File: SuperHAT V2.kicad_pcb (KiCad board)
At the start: 4 copper layers, 65 x 56.5 mm, 66 parts, among them J1 GPIO, J10 Qwiic_RA, J11 BM02B-GHS-TBT_LF__SN_, J13 SM02B-PASS-TBTLFSN, J2 Conn_01x03, J4 Conn_01x03, J5 Qwiic_RA, J6 Qwiic_Vertical, J7 Qwiic_Vertical, J8 SM04B-GHS-TB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

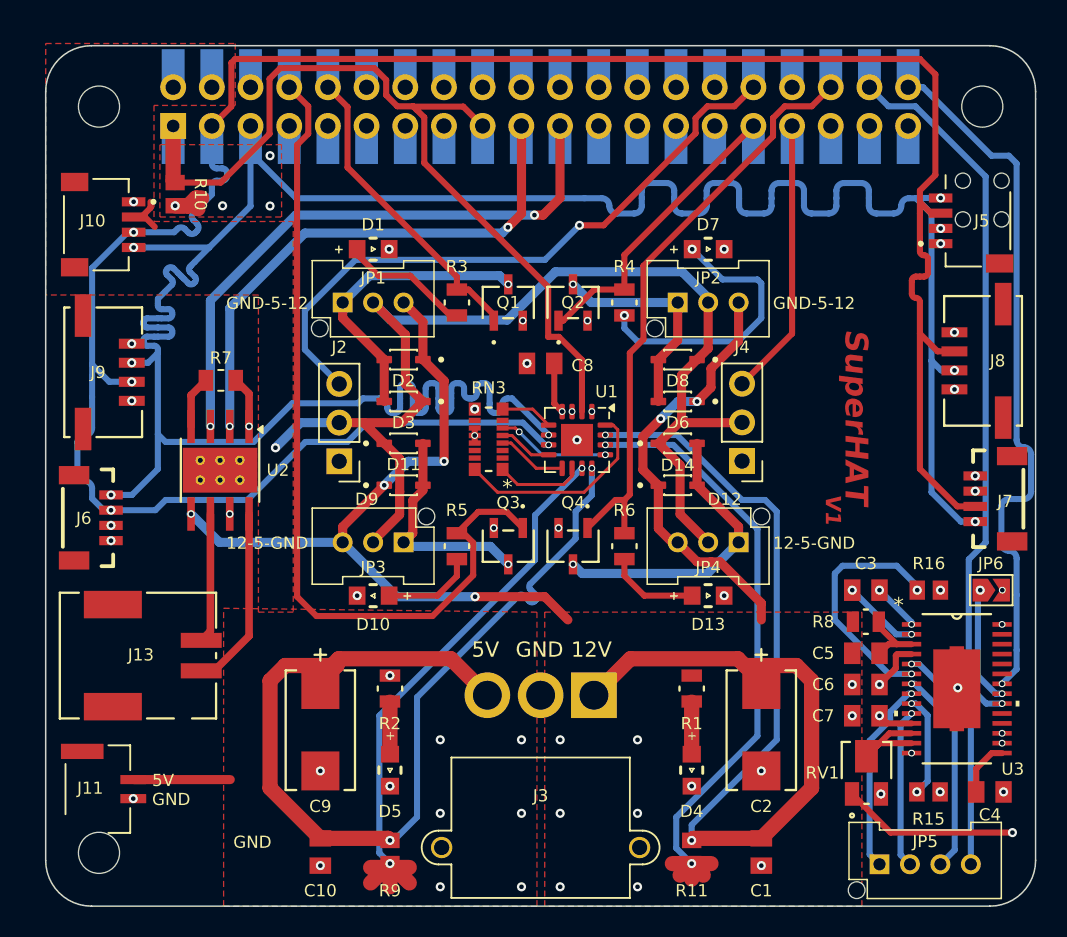
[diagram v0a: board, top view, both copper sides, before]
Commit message: Fixed MOSFET circuits, pin values, and diode layout.
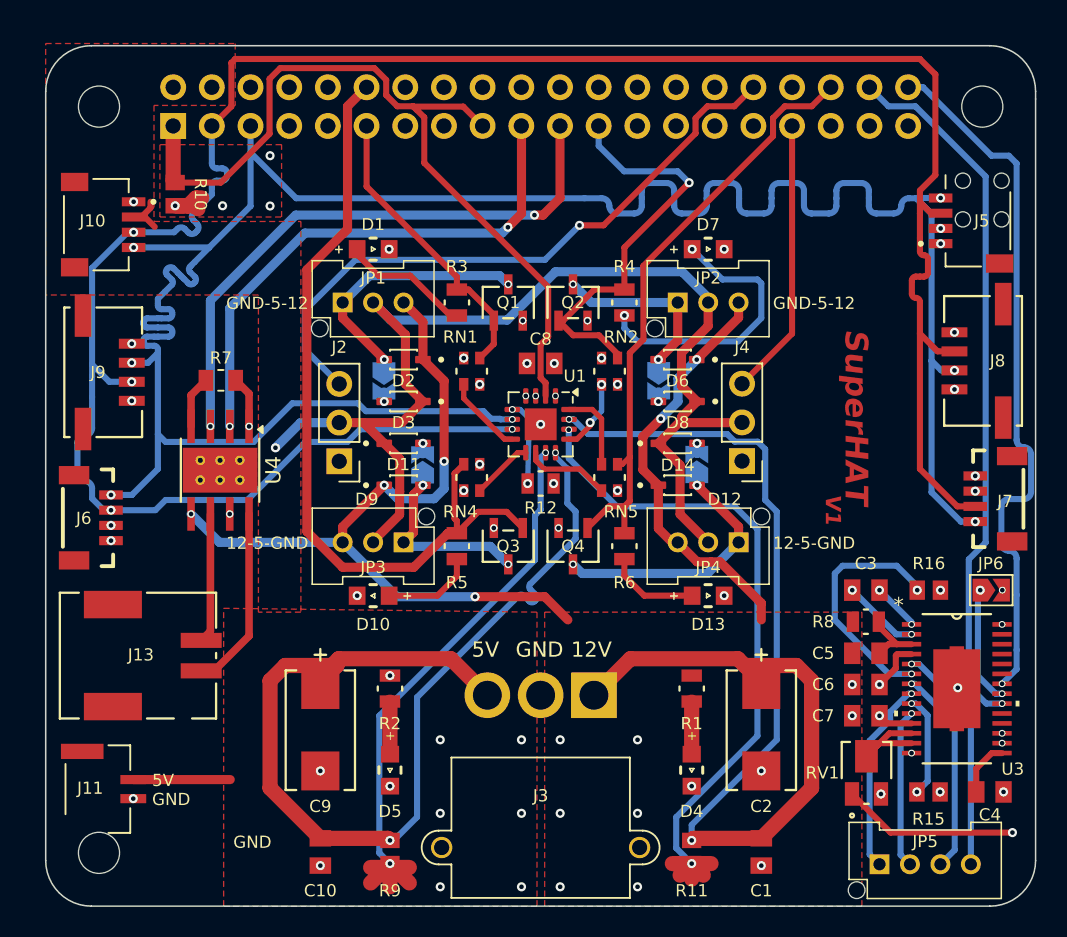
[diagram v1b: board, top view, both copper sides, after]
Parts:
- removed RN3: 10k, 10k Resistor Array:RES_EXB2HV
- removed U2: DRV8871DDA, Package_SO:Texas_HTSOP-8-1EP_3.9x4.9mm_P1.27mm_EP2.95x4.9mm_Mask2.4x3.1mm_ThermalVias
- added JP10: SolderJumper_2_Open, Jumper:SolderJumper-2_P1.3mm_Open_TrianglePad1.0x1.5mm, B.Cu at (142.8, 71.0)
- added JP7: SolderJumper_2_Open, Jumper:SolderJumper-2_P1.3mm_Open_TrianglePad1.0x1.5mm, B.Cu at (122.2, 65.5)
- added JP8: SolderJumper_2_Open, Jumper:SolderJumper-2_P1.3mm_Open_TrianglePad1.0x1.5mm, B.Cu at (140.2, 65.5)
- added JP9: SolderJumper_2_Open, Jumper:SolderJumper-2_P1.3mm_Open_TrianglePad1.0x1.5mm, B.Cu at (124.8, 71.0)
- added R12: 10k, 0805 Resistor Moisture Resistant:RES_CHP0805_BRN, F.Cu at (132.5, 72.2)
- added RN1: 10k, 2 RES 10k Array:SMT_1002P1AT_VIS, F.Cu at (128.0, 64.9)
- added RN2: 10k, 2 RES 10k Array:SMT_1002P1AT_VIS, F.Cu at (137.0, 64.9)
- added RN4: 10k, 2 RES 10k Array:SMT_1002P1AT_VIS, F.Cu at (128.0, 71.8)
- added RN5: 10k, 2 RES 10k Array:SMT_1002P1AT_VIS, F.Cu at (137.0, 71.8)
- added U4: DRV8871DDA, Package_SO:Texas_HTSOP-8-1EP_3.9x4.9mm_P1.27mm_EP2.95x4.9mm_Mask2.4x3.1mm_ThermalVias, F.Cu at (111.5, 71.4)
- moved D6 2.75 mm to (141.5, 64.1)
- moved D8 2.75 mm to (141.5, 66.9)
- moved U1 2.60 mm to (132.5, 68.4)
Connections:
- D11 pad A: Net-(Q3-D) -> Net-(JP9-B)
- D12 pad A: Net-(Q4-D) -> Net-(JP10-A)
- D14 pad A: Net-(Q4-D) -> Net-(JP10-B)
- D2 pad A: Net-(Q1-D) -> Net-(JP7-A)
- D3 pad A: Net-(Q1-D) -> Net-(JP7-B)
- D6 pad A: Net-(Q2-D) -> Net-(JP8-A)
- D8 pad A: Net-(Q2-D) -> Net-(JP8-B)
- D9 pad A: Net-(Q3-D) -> Net-(JP9-A)
- J1 pad 10: GPIO15/RXD0 -> /GPIO15/RXD0
- J1 pad 11: /GPIO17 -> GPIO17
- J1 pad 12: /GPIO18/PCM.CLK -> GPIO18/PCM.CLK
- J1 pad 23: /GPIO11/SPI0.SCLK -> GPIO11/SPI0.SCLK
- J1 pad 31: GPIO6 -> /GPIO6
- J1 pad 8: GPIO14/TXD0 -> /GPIO14/TXD0
- JP1 pad 1: Net-(Q1-D) -> Net-(JP7-A)
- JP2 pad 1: Net-(Q2-D) -> Net-(JP8-A)
- JP3 pad 1: Net-(Q3-D) -> Net-(JP9-A)
- JP4 pad 1: Net-(Q4-D) -> Net-(JP10-A)
- Q1 pad 1: GPIO15/RXD0 -> GPIO17
- Q1 pad 3: Net-(Q1-D) -> Net-(JP7-A)
- Q2 pad 1: GPIO6 -> GPIO11/SPI0.SCLK
- Q2 pad 3: Net-(Q2-D) -> Net-(JP8-A)
- Q3 pad 1: GPIO14/TXD0 -> GPIO18/PCM.CLK
- Q3 pad 3: Net-(Q3-D) -> Net-(JP9-A)
- Q4 pad 3: Net-(Q4-D) -> Net-(JP10-A)
- R3 pad 1: GPIO15/RXD0 -> GPIO17
- R4 pad 1: GPIO6 -> GPIO11/SPI0.SCLK
- R5 pad 1: GPIO14/TXD0 -> GPIO18/PCM.CLK
- U1 pad 10: Net-(RN3-R1.1) -> /PV
- U1 pad 13: Net-(RN3-R6.1) -> /TC
- U1 pad 16: Net-(RN3-R1.2) -> /VPU
- U1 pad 8: Net-(RN3-R5.1) -> /WARNING
- U1 pad 9: Net-(RN3-R4.1) -> /CRITICAL
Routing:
- net GPIO14/TXD0: track 56.3 -> 0.00 mm
- net GPIO18/PCM.CLK: track 0.00 -> 53.2 mm
- net GPIO11/SPI0.SCLK: track 0.00 -> 27.2 mm, vias 0 -> 1
- net GPIO15/RXD0: track 20.3 -> 0.00 mm
- net Net-(Q4-D): track 19.6 -> 0.00 mm, vias 1 -> 0
- net GPIO17: track 0.00 -> 19.5 mm
- net Net-(Q1-D): track 19.5 -> 0.00 mm, vias 1 -> 0
- net GPIO6: track 19.4 -> 0.00 mm
- net Net-(JP10-A): track 0.00 -> 17.5 mm, vias 0 -> 2
- net Net-(JP7-A): track 0.00 -> 17.4 mm, vias 0 -> 2
- net Net-(Q3-D): track 14.5 -> 0.00 mm, vias 1 -> 0
- net Net-(Q2-D): track 14.4 -> 0.00 mm, vias 1 -> 0
- net /GPIO3/SCL1: track 169.6 -> 155.3 mm
- net Net-(RN3-R1.2): track 13.8 -> 0.00 mm
- net Net-(JP9-A): track 0.00 -> 12.4 mm, vias 0 -> 2
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
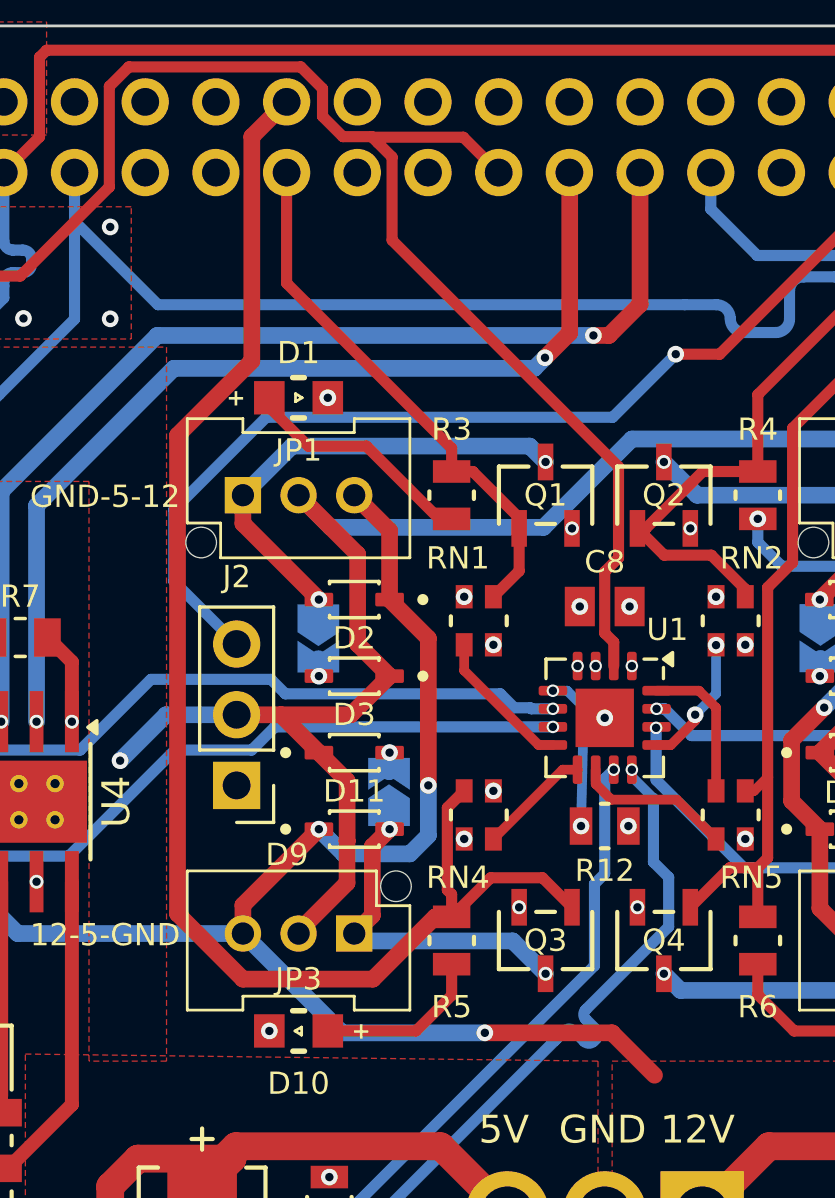
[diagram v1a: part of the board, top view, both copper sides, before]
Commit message: Added overvoltage protection to schematic.
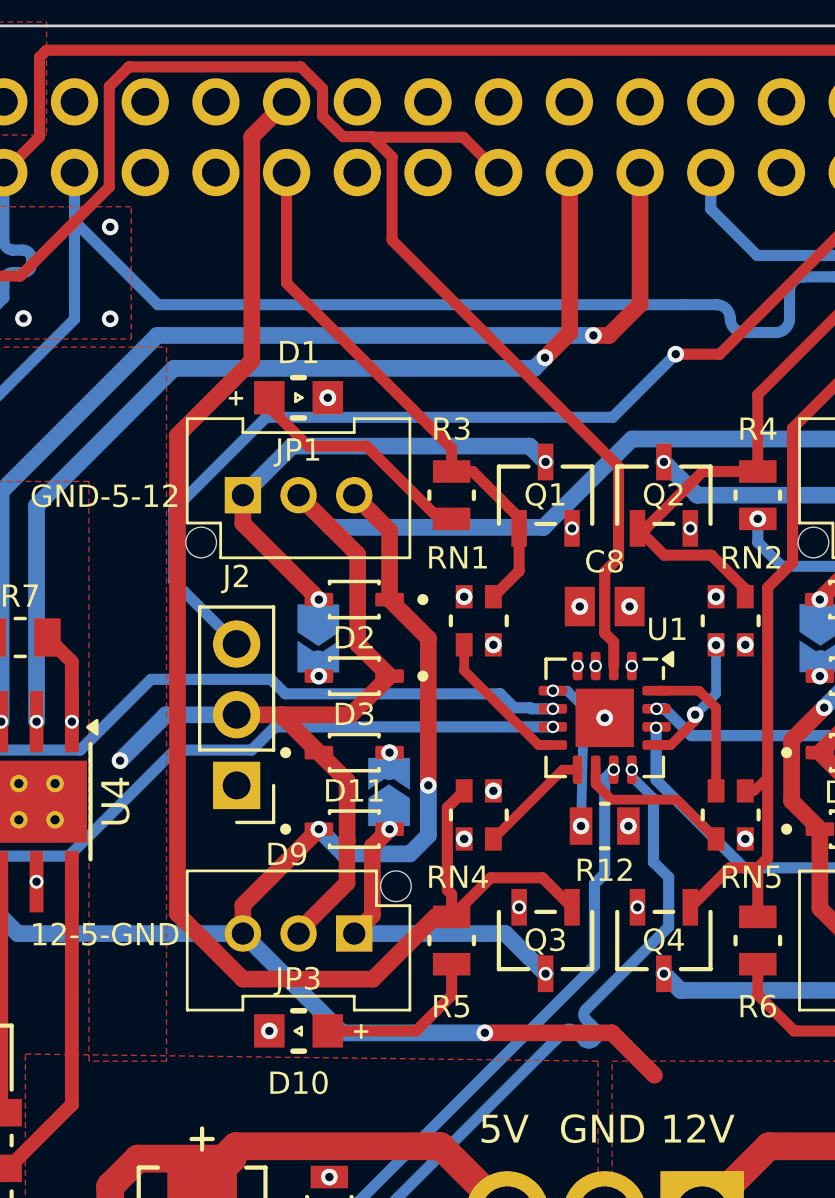
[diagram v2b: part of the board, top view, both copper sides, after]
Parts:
- R3, R4, R5, R6: value 33 -> 100; footprint CMP0805AFX:RES_CMP0805_BRN -> 0805 Resistor Moisture Resistant:RES_CHP0805_BRN

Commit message: Overvoltage protection laid out on footprint.
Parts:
- removed J13: SM02B-PASS-TBTLFSN, SM02B-PASS-TBT:CONN_SM02B-PASS_JST
- added C11: 10 nF, 0805 Ceramic Capacitor:CAPC2012X140N, F.Cu at (108.0, 91.5)
- added C12: 0.1 uF, 0805 Ceramic Capacitor:CAPC2012X140N, F.Cu at (108.5, 57.1)
- added J12: B02B-PASK-1, B02B-PASK-1:CONN_B02B-PASK-1_JST, F.Cu at (104.2, 83.0)
- added R13: 10k, 0805 Resistor Moisture Resistant:RES_CHP0805_BRN, F.Cu at (102.9, 98.2)
- added R14: 453, RESC2012X60N:RESC2012X60N, F.Cu at (107.2, 98.2)
- added R17: 470k, CMP0805AFX:RES_CMP0805_BRN, F.Cu at (108.0, 95.2)
- added R18: 7.5k, TNPW0805:RES_TNPW0805_VIS, F.Cu at (102.9, 88.3)
- added R19: 2.4k, TNPW0805:RES_TNPW0805_VIS, F.Cu at (107.3, 88.3)
- added U2: TPS259631DDAR, TPS259631:SOIC_20DDAR_TEX, F.Cu at (103.8, 93.3)
- J11: value BM02B-GHS-TBT_LF__SN_ -> Conn_01x02; footprint BM02B-GHS-TBT:BM02B-GHS-TBT -> Connector_PinHeader_2.54mm:PinHeader_1x02_P2.54mm_Horizontal
- moved J11 13.1 mm to (115.0, 95.6)
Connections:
- J1 pad 2: +5V -> +5VPI
- J1 pad 4: +5V -> +5VPI
- J10 pad 2: +5V -> +5VPI
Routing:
- net /GPIO27: track 0.00 -> 82.5 mm, vias 0 -> 1
- net +5V: track 125.7 -> 114.6 mm
- net Net-(U2-EN/UVLO): track 0.00 -> 5.02 mm
- net Net-(U2-DVDT): track 0.00 -> 4.49 mm
- net +3V3: track 15.1 -> 19.4 mm, vias 19 -> 21
- net Net-(U2-ILM): track 0.00 -> 2.98 mm
- net Net-(U4-OUT1): track 8.55 -> 10.9 mm
- net Net-(U2-OVCSEL): track 0.00 -> 2.25 mm
- net Net-(U4-OUT2): track 12.1 -> 14.0 mm
- net GND: track 3.39 -> 4.89 mm, vias 40 -> 46
- net +5VPI: track 0.00 -> 1.25 mm
- added copper zone on F.Cu, net +5VPI
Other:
- outline, holes or cut-outs redrawn
- board text added: "V2"

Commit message: Pre footprint migration to create BOM V2
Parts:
- R1: value 1k -> 3k; footprint 0805 Resistor Moisture Resistant:RES_CHP0805_BRN -> TNPW0805:RES_TNPW0805_VIS
- R2: value 330 -> 1k; footprint 0805 330 Ohm Resistor Moisture Resistant:RES_CMP0805_BRN -> TNPW0805:RES_TNPW0805_VIS
- moved R1 0.29 mm to (142.4, 86.0)
- moved R2 0.29 mm to (122.6, 86.0)
- moved D4 0.22 mm to (142.4, 91.3)
- moved D5 0.22 mm to (122.6, 91.3)
- moved D10 0.20 mm to (121.5, 79.8)
- moved D13 0.20 mm to (143.5, 79.8)
- moved D1 0.20 mm to (121.5, 56.7)
- moved D7 0.20 mm to (143.5, 56.7)
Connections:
- U3 pad 20: /GPIO20/PCM.DIN -> /GPIO26
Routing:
- net /GPIO20/PCM.DIN: track 46.6 -> 0.00 mm, vias 1 -> 0
- net /GPIO26: track 0.00 -> 44.3 mm, vias 0 -> 1
- net /GPIO3/SCL1: track 155.3 -> 167.1 mm
- net +5VPI: track 1.25 -> 8.03 mm
- net +12V: track 130.4 -> 131.6 mm, vias 16 -> 17
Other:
- board text removed: "V1"

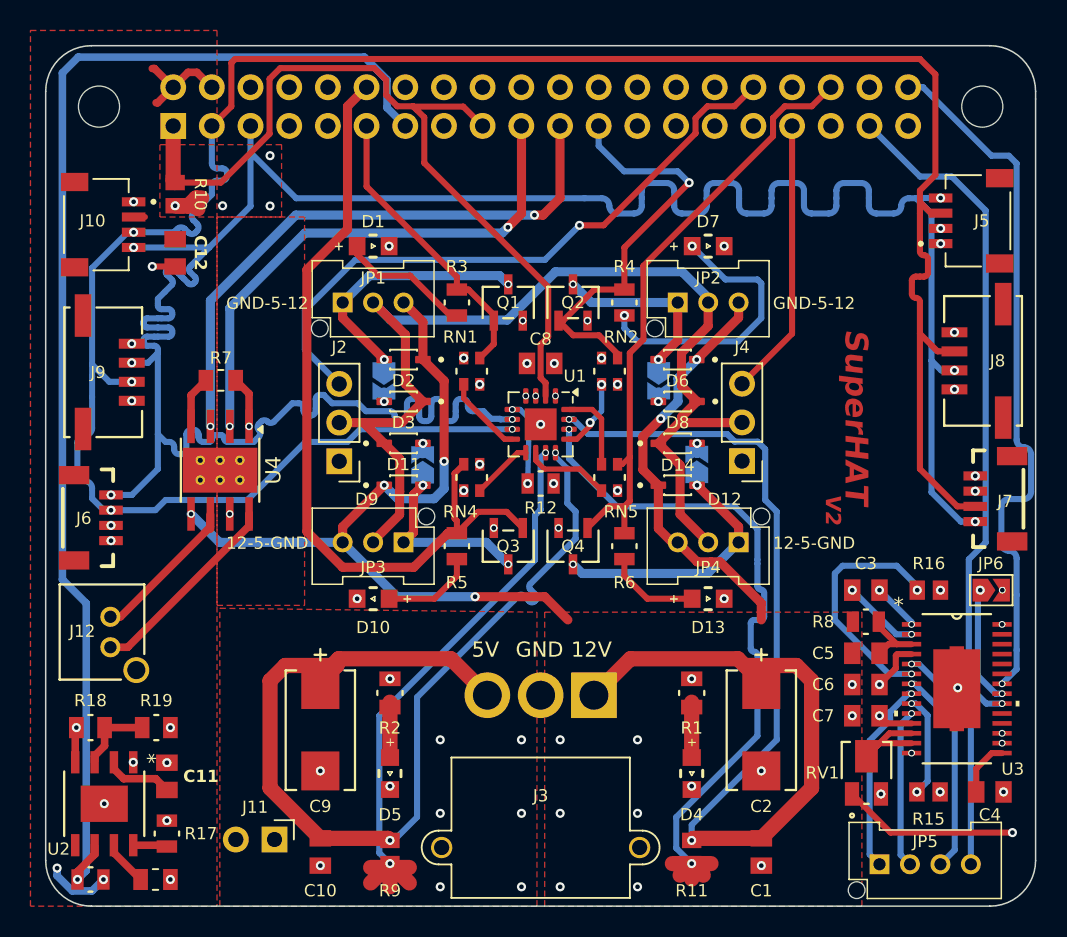
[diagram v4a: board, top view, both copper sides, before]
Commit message: Bom acting goofy but I still generated one.
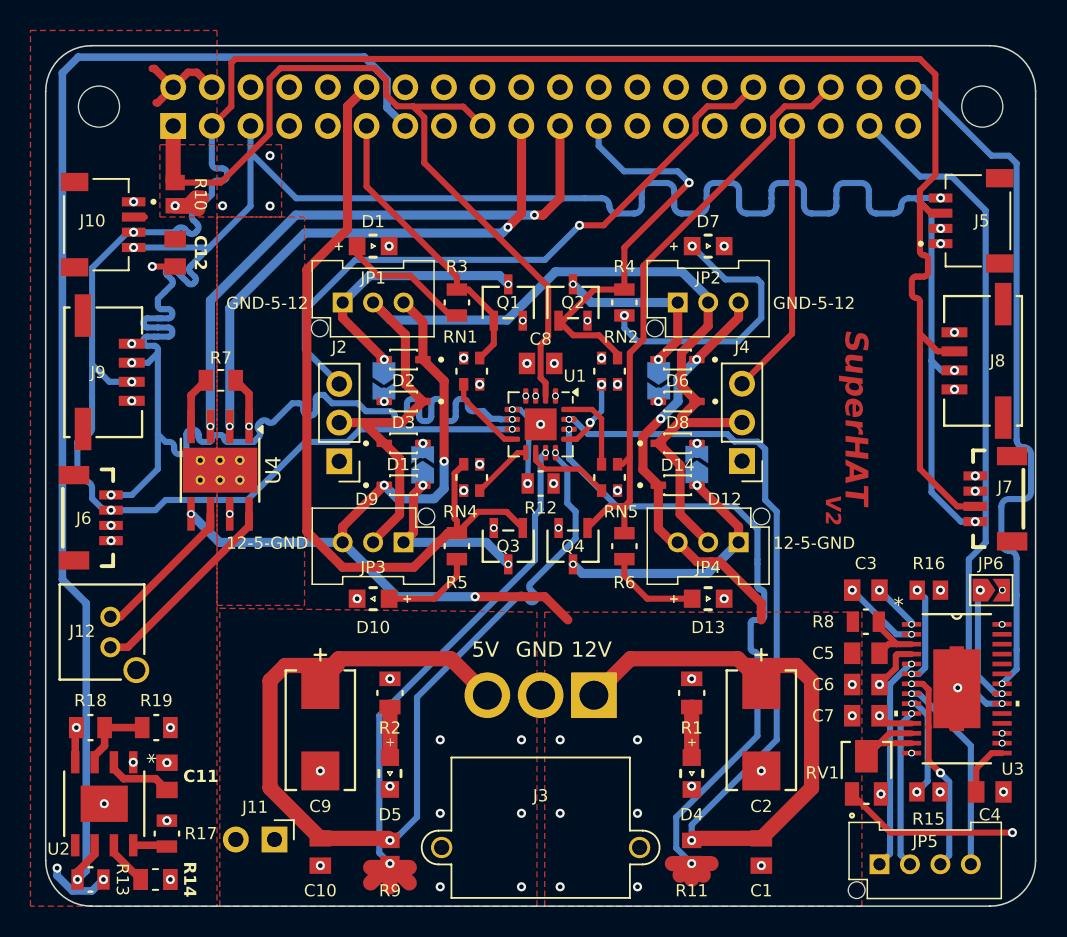
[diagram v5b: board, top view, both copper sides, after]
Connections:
- JP5 pad 1: Net-(U3-BOUT2) -> Net-(U3-AOUT1)
- JP5 pad 4: Net-(U3-AOUT1) -> Net-(U3-BOUT2)
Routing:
- net Net-(U3-ISENA): track 16.0 -> 6.37 mm
- net Net-(U3-AOUT1): track 15.0 -> 14.1 mm
- net Net-(U3-AOUT2): track 13.5 -> 13.6 mm, vias 1 -> 2
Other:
- board text added: "V2.0 2/2025 By Harry O'Hagin"
- board text removed: "V1.0 12/2024 By Harry O'Hagin"

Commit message: SuperHAT V2
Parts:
- R19: value 2.4k -> 2.61k
- U2: value TPS259631DDAR -> TPS259621DDAR
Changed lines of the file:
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@@
 		(grid_origin 100 100)
 		(pcbplotparams
-			(layerselection 0x000000c_7ffffff8)
+			(layerselection 0x00010fc_ffffffff)
 			(plot_on_all_layers_selection 0x0000000_00000000)
 			(disableapertmacros no)
-			(usegerberextensions no)
+			(usegerberextensions yes)
 			(usegerberattributes no)
 			(usegerberadvancedattributes no)
-			(creategerberjobfile yes)
+			(creategerberjobfile no)
 			(dashed_line_dash_ratio 12.000000)
 			(dashed_line_gap_ratio 3.000000)
@@
 			(plotinvisibletext no)
 			(sketchpadsonfab no)
-			(subtractmaskfromsilk no)
+			(subtractmaskfromsilk yes)
 			(outputformat 1)
 			(mirror no)
@@
 			)
 		)
-		(property "Value" "TPS259631DDAR"
+		(property "Value" "TPS259621DDAR"
 			(at 0 0 -90)
 			(unlocked yes)
@@
 			)
 		)
-		(property "Value" "2.4k"
+		(property "Value" "2.61k"
 			(at 0 0 0)
 			(unlocked yes)
@@
 			)
 		)
-		(property "Description" "RES 2.4K OHM 0.1% 0.26W 0805"
+		(property "Description" "RES 2.61K OHM 0.1% 0.26W 0805"
 			(at 0 0 0)
 			(layer "F.Fab")
@@
 			)
 		)
-		(property "Part #" "TNPW08052K40BEEA"
+		(property "Part #" "TNPW08052K61BEEN"
 			(at 0 0 0)
 			(unlocked yes)
@@
 			)
 		)
-		(property "Order Link" "https://www.digikey.com/en/products/detail/vishay-dale/TNPW08052K40BEEA/1607323"
+		(property "Order Link" "https://www.digikey.com/en/products/detail/vishay-dale/TNPW08052K61BEEN/1610534?s=N4IgjCBcoEwAwA4CsVQGMoDMCGAbAzgKYA0IA9lANogwB0AbGAAQDWA8gBYC2%2BIAuqQAOAFyggAqgDsAlsLaYAsoWz4ArgCdCIAL6kAtDFQgMkYetUlyVECj7bdNawBUAcgAUA6oji3tQA"
 			(at 0 0 0)
 			(unlocked yes)
@@
 			)
 		)
-		(property "Price" "$0.39"
+		(property "Price" "$0.67"
 			(at 0 0 0)
 			(unlocked yes)
